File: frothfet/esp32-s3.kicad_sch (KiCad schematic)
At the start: 29 parts, among them J13 USB_TYPE_C_16PIN, J14 Conn_01x04, SW1 BOOT, SW2 RESET, U30 ESP32-S3-WROOM-1-N16R8, U31 USBLC6-2SC6, U32 SN74LV1T34DBV, U33 XC6210B332MR

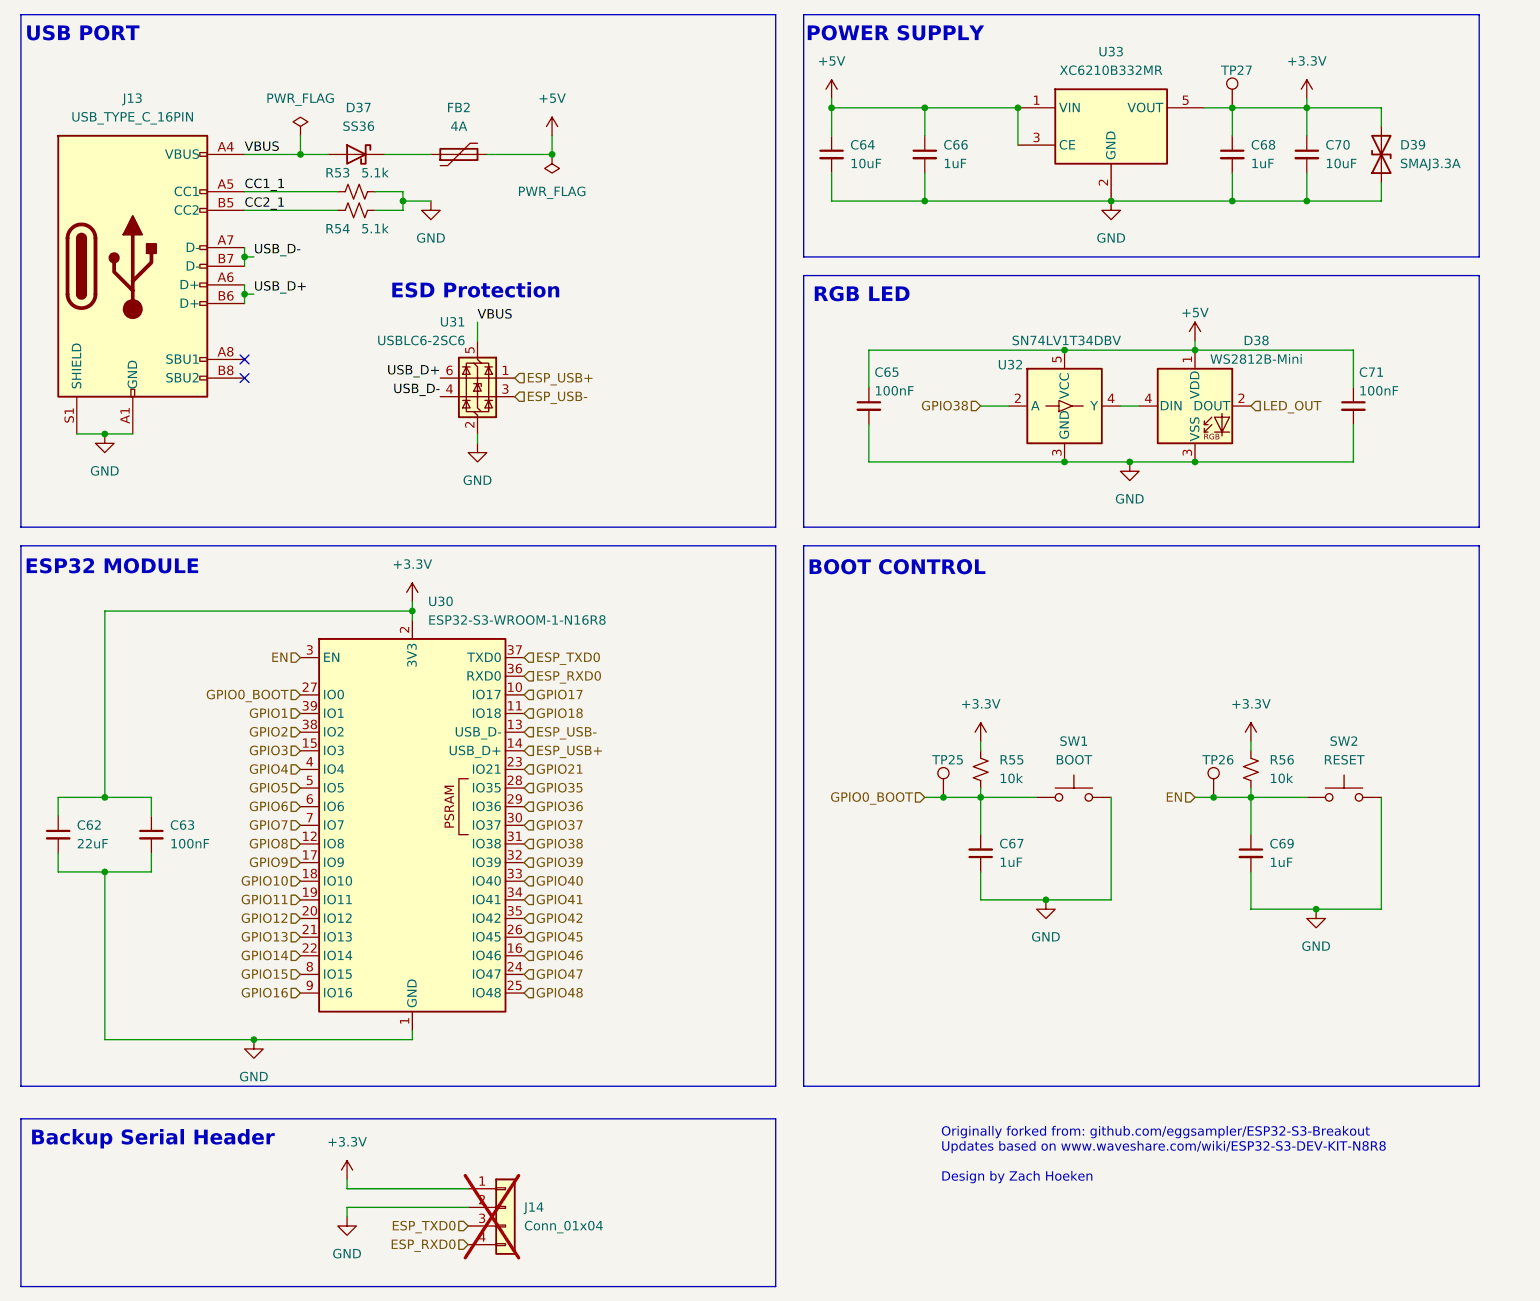
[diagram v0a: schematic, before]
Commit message: added support for ALERT pin from INA226 for overcurrent protection (hopefully)
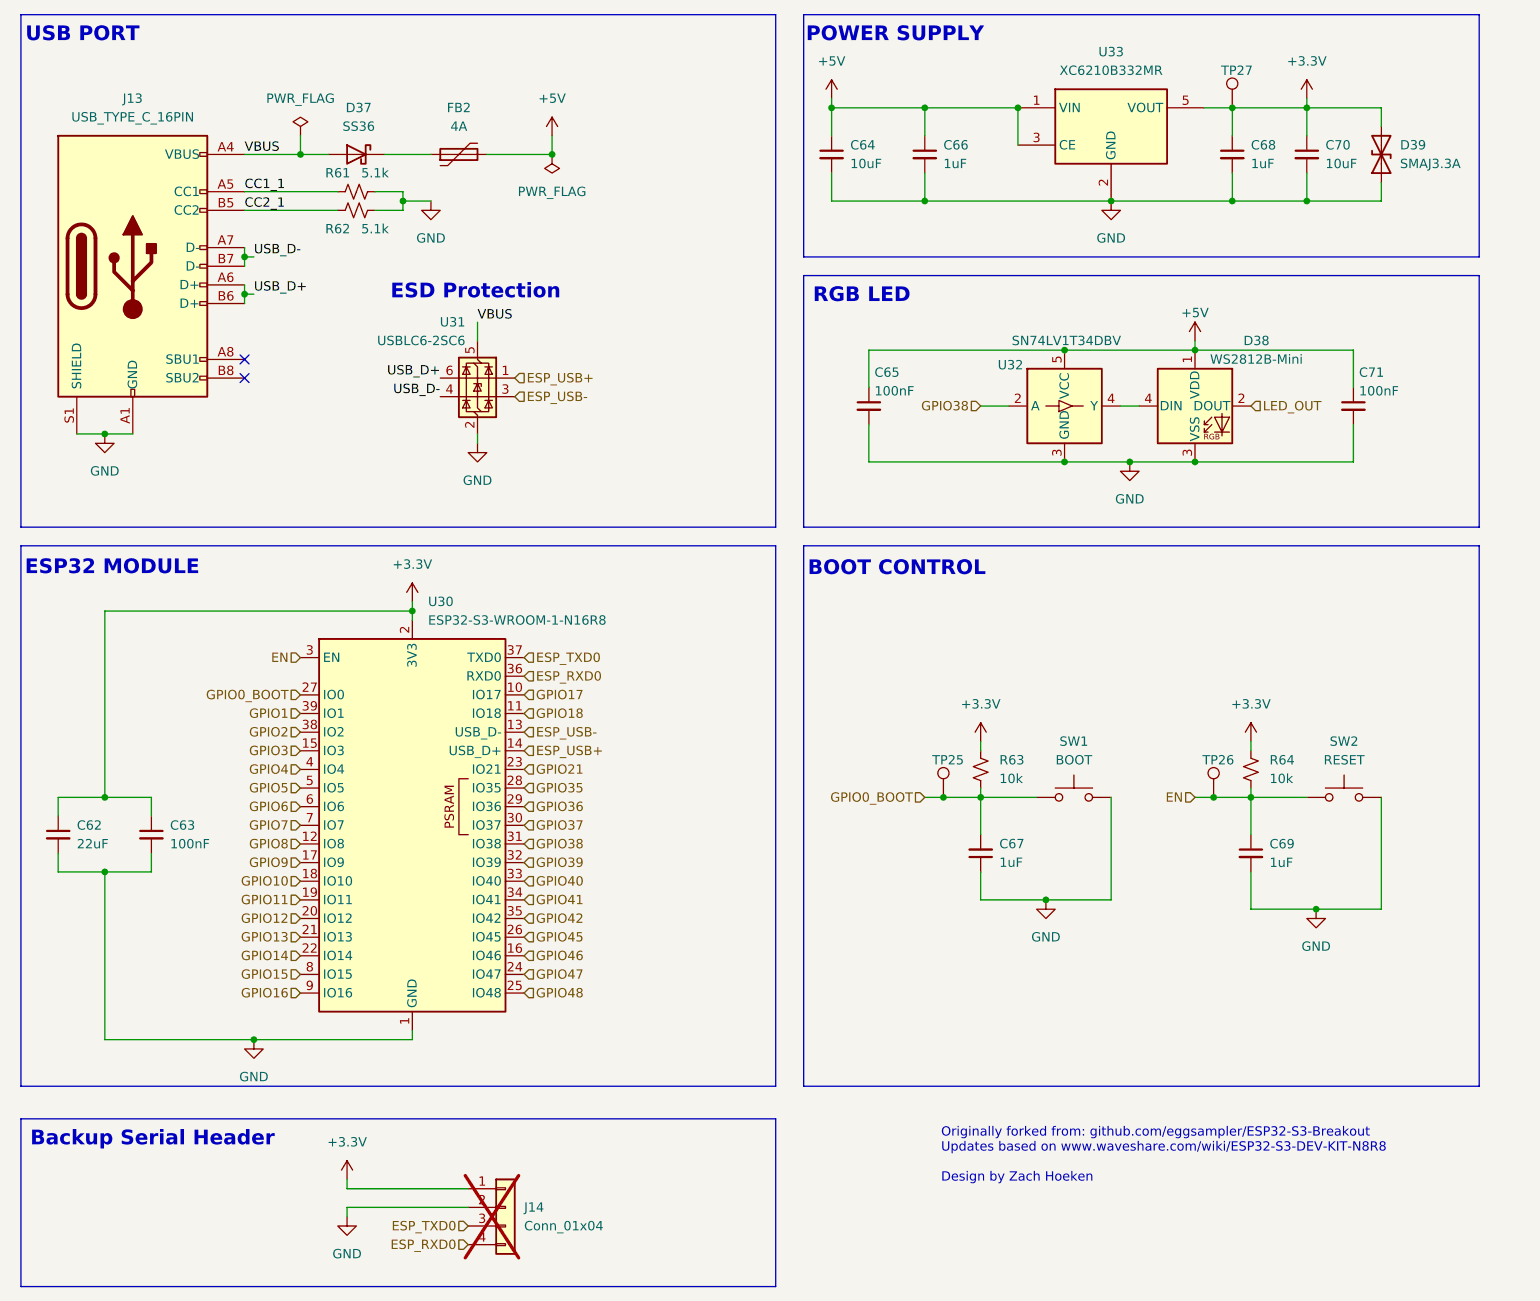
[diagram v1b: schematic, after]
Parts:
- renumbered R53 to R61, R54 to R62, R55 to R63, R56 to R64
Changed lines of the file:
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@@
 		(dnp no)
 		(fields_autoplaced yes)
-		(property "Reference" "#FLG010"
+		(property "Reference" "#FLG09"
 			(at 125.73 37.465 0)
 			(effects
@@
 			(project "frothfet"
 				(path "/c83c6236-96e9-46ad-9d7a-9e2efa4a7966/777fe0ac-daa5-4cfe-9bd1-5eba0a425019"
-					(reference "#FLG010")
+					(reference "#FLG09")
 					(unit 1)
 				)
@@
 		(on_board yes)
 		(dnp no)
-		(property "Reference" "R54"
+		(property "Reference" "R62"
 			(at 96.52 45.72 90)
 			(effects
@@
 			(project "frothfet"
 				(path "/c83c6236-96e9-46ad-9d7a-9e2efa4a7966/777fe0ac-daa5-4cfe-9bd1-5eba0a425019"
-					(reference "R54")
+					(reference "R62")
 					(unit 1)
 				)
@@
 		(dnp no)
 		(fields_autoplaced yes)
-		(property "Reference" "#FLG09"
+		(property "Reference" "#FLG08"
 			(at 91.44 31.115 0)
 			(effects
@@
 			(project "frothfet"
 				(path "/c83c6236-96e9-46ad-9d7a-9e2efa4a7966/777fe0ac-daa5-4cfe-9bd1-5eba0a425019"
-					(reference "#FLG09")
+					(reference "#FLG08")
 					(unit 1)
 				)
@@
 		(dnp no)
 		(fields_autoplaced yes)
-		(property "Reference" "R55"
+		(property "Reference" "R63"
 			(at 186.69 118.1099 0)
 			(effects
@@
 			(project "frothfet"
 				(path "/c83c6236-96e9-46ad-9d7a-9e2efa4a7966/777fe0ac-daa5-4cfe-9bd1-5eba0a425019"
-					(reference "R55")
+					(reference "R63")
 					(unit 1)
 				)
@@
 		(on_board yes)
 		(dnp no)
-		(property "Reference" "R53"
+		(property "Reference" "R61"
 			(at 96.52 38.1 90)
 			(effects
@@
 			(project "frothfet"
 				(path "/c83c6236-96e9-46ad-9d7a-9e2efa4a7966/777fe0ac-daa5-4cfe-9bd1-5eba0a425019"
-					(reference "R53")
+					(reference "R61")
 					(unit 1)
 				)
@@
 		(dnp no)
 		(fields_autoplaced yes)
-		(property "Reference" "R56"
+		(property "Reference" "R64"
 			(at 223.52 118.1099 0)
 			(effects
@@
 			(project "frothfet"
 				(path "/c83c6236-96e9-46ad-9d7a-9e2efa4a7966/777fe0ac-daa5-4cfe-9bd1-5eba0a425019"
-					(reference "R56")
+					(reference "R64")
 					(unit 1)
 				)

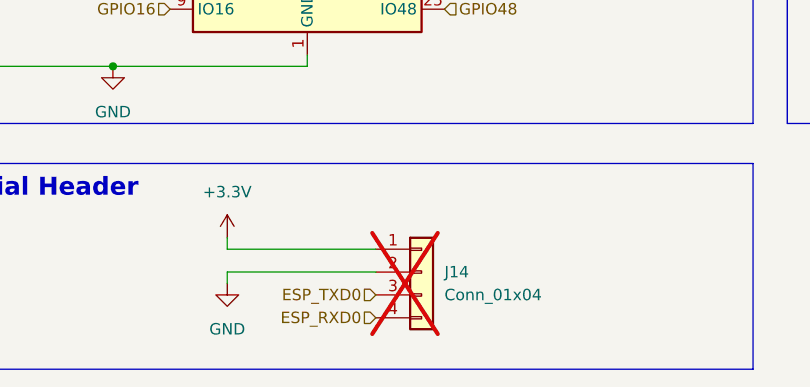
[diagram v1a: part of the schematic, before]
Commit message: rearranged the buttons
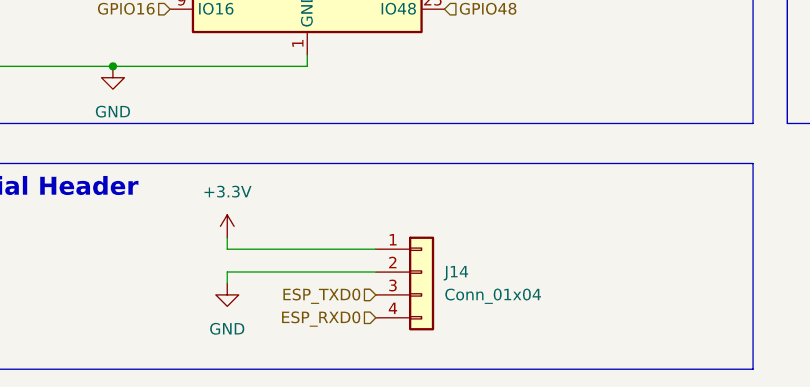
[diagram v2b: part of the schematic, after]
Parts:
- J14: now fitted
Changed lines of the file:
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@@
 		(in_bom yes)
 		(on_board yes)
-		(dnp yes)
+		(dnp no)
 		(fields_autoplaced yes)
 		(property "Reference" "J14"
